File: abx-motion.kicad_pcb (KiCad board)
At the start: 4 copper layers, 157 x 105 mm, 203 parts, among them J1 XT60_BAT, J102 E_STOP, J201 USB-C, J202 ENC1_CONN, J203 ENC2_CONN, J204 CAN_TERM, J205 CAN_BUS, J206 RS485_TERM, J207 RS485_BUS, J208 OLED_I2C, J209 I2C_EXP, J301 MOTOR_OUT, J401 MOTOR_OUT, J501 STEP1_MOTOR, J502 STEP1_EXT, J503 STEP2_MOTOR, J504 STEP2_EXT, J505 RELAY1_OUT, J506 RELAY2_OUT, K501 G5LE-14-DC5, K502 G5LE-14-DC5, Q1 SQJ459EP-T1_GE3, Q301 CSD18540Q5B, Q302 CSD18540Q5B, Q303 CSD18540Q5B, Q304 CSD18540Q5B, Q401 CSD18540Q5B, Q402 CSD18540Q5B, Q403 CSD18540Q5B, Q404 CSD18540Q5B, Q501 AO3400A, Q502 AO3400A, SW201 RESET, SW202 BOOT, SW203 BTN_BACK, SW204 BTN_NEXT, SW205 BTN_HOME, SW501 MICROSTEP_CFG, SW502 MICROSTEP_CFG, U1 LMR36520FADDA, U2 AP2112K-3.3, U201 USBLC6-2SC6, U202 TCAN1042V-Q1, U203 THVD1450DR, U3 ESP32-S3-WROOM-1-N8R2, U301 DRV8701ERGER, U4 74LVC14A, U401 DRV8701ERGER, U501 StepStick_DRV8825, U502 StepStick_DRV8825

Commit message: Resolve all 5 prototype review items (F1 3557-2 4-pad THT, SMCJ30A, 2.2nF/0.5W snubber, 0.45-0.50mm stepper traces, clean PTH/NPTH drills)
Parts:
- C310, C410: value 10nF -> 2.2nF
- D2: value SMCJ28A -> SMCJ30A
- moved F1 5.55 mm to (167.6, 54.0)
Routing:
- net /Power_Supply/V_RAW_IN: track 32.2 -> 24.7 mm
- net /Power_Supply/V_FUSED: track 12.7 -> 17.7 mm
- net /Steppers_and_Relays/STEP2_A1: track 30.6 -> 31.5 mm
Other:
- board text added: "VBAT (J1 XT60): 12-32V (25A Fuse, Rev-Prot, SMCJ30A)"
- board text removed: "VBAT (J1 XT60): 12-32V (25A Fuse, Rev-Prot, SMCJ28A)"

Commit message: Release v1.0-production: finalize F1 3D STEP model alignment and archive V1.0 production package
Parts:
- F1: footprint Fuse:Fuse_Blade_ATO_directSolder -> abx-footprints:Fuseholder_Keystone_3557-2
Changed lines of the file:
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@@
 		)
 	)
-	(footprint "Fuse:Fuse_Blade_ATO_directSolder"
+	(footprint "abx-footprints:Fuseholder_Keystone_3557-2"
 		(layer "F.Cu")
 		(at 167.55 54)
@@
 		)
 		(embedded_fonts no)
-		(model "${KICAD9_3DMODEL_DIR}/Fuse.3dshapes/Fuseholder_Blade_Mini_Keystone_3568.step"
+		(model "${KIPRJMOD}/3dmodels/Fuseholder_Keystone_3557-2.step"
 			(offset
 				(xyz 0 0 0)

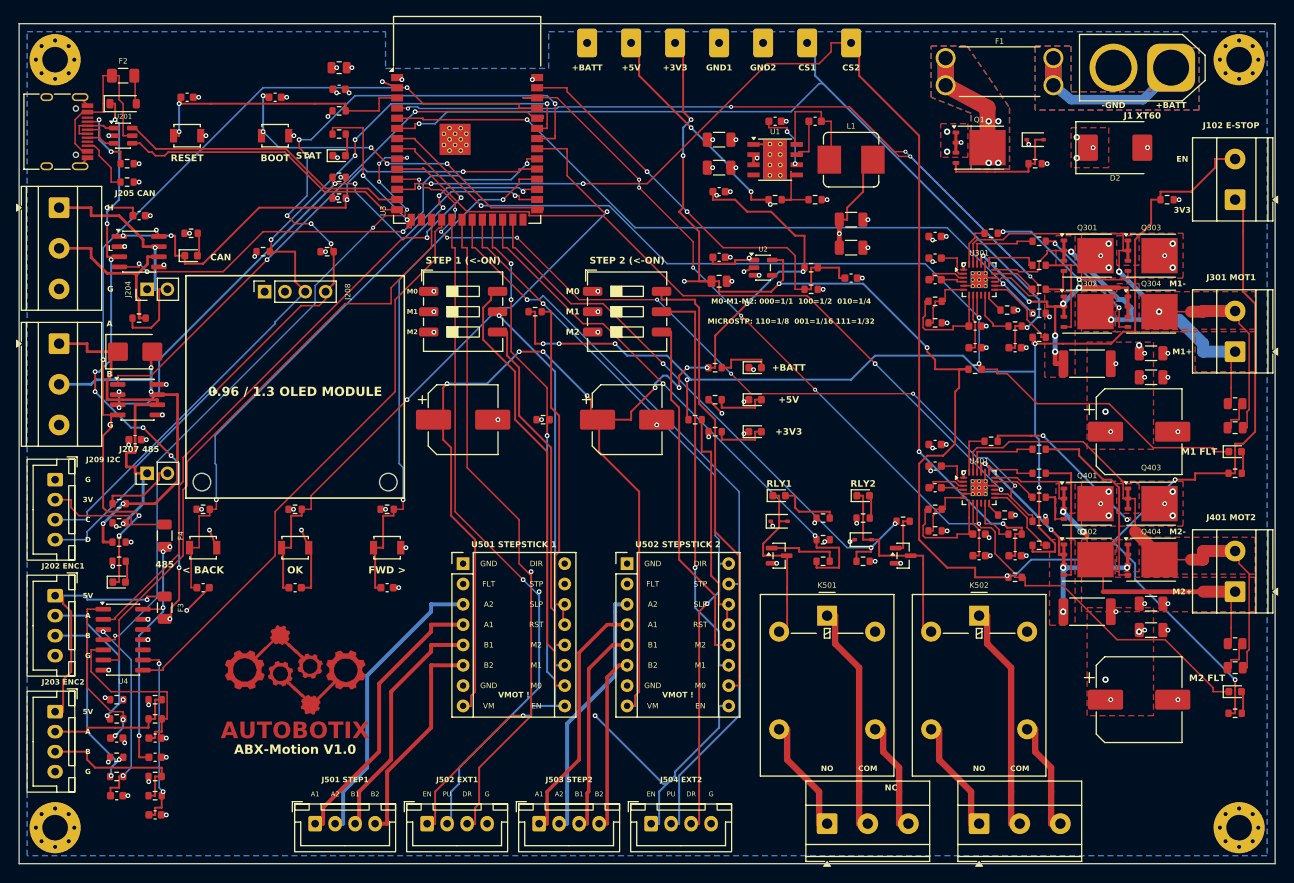
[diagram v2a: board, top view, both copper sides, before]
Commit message: Complete V1.1 compact 6-channel I/O & DC output architecture (0 ERC, 0 DRC errors, 0 unconnected, 0 parity)
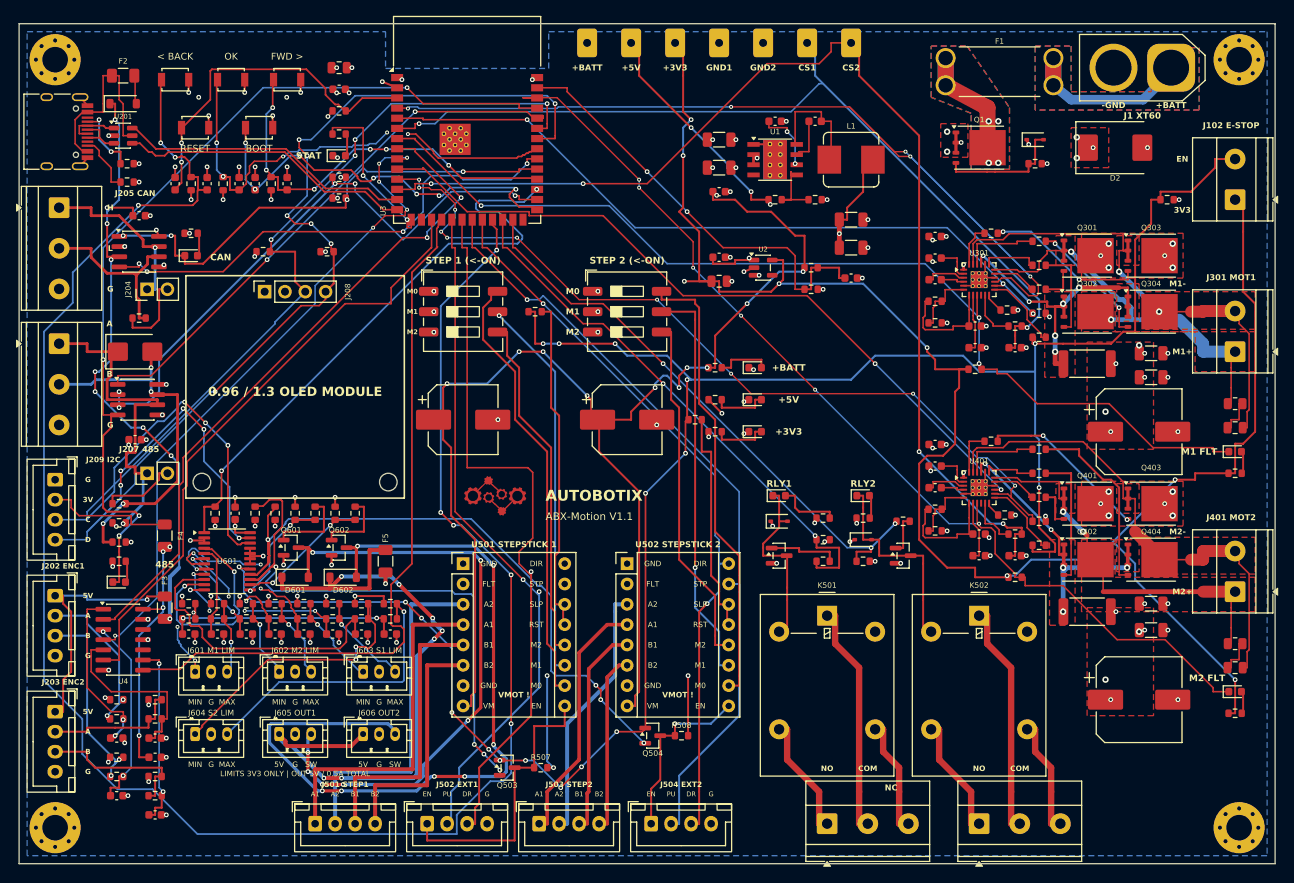
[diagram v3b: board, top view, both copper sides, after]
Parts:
- added C601: 100nF, Capacitor_SMD:C_0603_1608Metric, F.Cu at (72.0, 109.2)
- added C602: 10nF, Capacitor_SMD:C_0603_1608Metric, F.Cu at (66.2, 124.3)
- added C603: 10nF, Capacitor_SMD:C_0603_1608Metric, F.Cu at (69.8, 124.3)
- added C604: 10nF, Capacitor_SMD:C_0603_1608Metric, F.Cu at (73.4, 124.3)
- added C605: 10nF, Capacitor_SMD:C_0603_1608Metric, F.Cu at (77.0, 124.3)
- added C606: 10nF, Capacitor_SMD:C_0603_1608Metric, F.Cu at (80.6, 124.3)
- added C607: 10nF, Capacitor_SMD:C_0603_1608Metric, F.Cu at (84.2, 124.3)
- added C608: 10nF, Capacitor_SMD:C_0603_1608Metric, F.Cu at (87.8, 124.3)
- added C609: 10nF, Capacitor_SMD:C_0603_1608Metric, F.Cu at (91.4, 124.3)
- added D601: B5819W, Diode_SMD:D_SOD-123, F.Cu at (79.5, 117.2)
- added D602: B5819W, Diode_SMD:D_SOD-123, F.Cu at (85.5, 117.2)
- added F5: 500mA_PTC, Fuse:Fuse_1206_3216Metric, F.Cu at (90.8, 115.2)
- added J601: B3B-PH-K-S, Connector_JST:JST_PH_B3B-PH-K_1x03_P2.00mm_Vertical, F.Cu at (67.0, 129.0)
- added J602: B3B-PH-K-S, Connector_JST:JST_PH_B3B-PH-K_1x03_P2.00mm_Vertical, F.Cu at (77.5, 129.0)
- added J603: B3B-PH-K-S, Connector_JST:JST_PH_B3B-PH-K_1x03_P2.00mm_Vertical, F.Cu at (88.0, 129.0)
- added J604: B3B-PH-K-S, Connector_JST:JST_PH_B3B-PH-K_1x03_P2.00mm_Vertical, F.Cu at (67.0, 136.8)
- added J605: B3B-PH-K-S, Connector_JST:JST_PH_B3B-PH-K_1x03_P2.00mm_Vertical, F.Cu at (77.5, 136.8)
- added J606: B3B-PH-K-S, Connector_JST:JST_PH_B3B-PH-K_1x03_P2.00mm_Vertical, F.Cu at (88.0, 136.8)
- added Q503: AO3400A, Package_TO_SOT_SMD:SOT-23, F.Cu at (106.0, 141.0)
- added Q504: AO3400A, Package_TO_SOT_SMD:SOT-23, F.Cu at (124.2, 137.0)
- added Q601: AO3400A, Package_TO_SOT_SMD:SOT-23, F.Cu at (79.0, 113.5)
- added Q602: AO3400A, Package_TO_SOT_SMD:SOT-23, F.Cu at (85.0, 113.5)
- added R507: 10k, Resistor_SMD:R_0603_1608Metric, F.Cu at (110.2, 141.0)
- added R508: 10k, Resistor_SMD:R_0603_1608Metric, F.Cu at (127.8, 137.0)
- added R601: 4.7k, Resistor_SMD:R_0603_1608Metric, F.Cu at (66.2, 120.5)
- added R602: 4.7k, Resistor_SMD:R_0603_1608Metric, F.Cu at (69.8, 120.5)
- added R603: 4.7k, Resistor_SMD:R_0603_1608Metric, F.Cu at (73.4, 120.5)
- added R604: 4.7k, Resistor_SMD:R_0603_1608Metric, F.Cu at (77.0, 120.5)
- added R605: 4.7k, Resistor_SMD:R_0603_1608Metric, F.Cu at (80.6, 120.5)
- added R606: 4.7k, Resistor_SMD:R_0603_1608Metric, F.Cu at (84.2, 120.5)
- added R607: 4.7k, Resistor_SMD:R_0603_1608Metric, F.Cu at (87.8, 120.5)
- added R608: 4.7k, Resistor_SMD:R_0603_1608Metric, F.Cu at (91.4, 120.5)
- added R609: 1k, Resistor_SMD:R_0603_1608Metric, F.Cu at (66.2, 122.4)
- added R610: 1k, Resistor_SMD:R_0603_1608Metric, F.Cu at (69.8, 122.4)
- added R611: 1k, Resistor_SMD:R_0603_1608Metric, F.Cu at (73.4, 122.4)
- added R612: 1k, Resistor_SMD:R_0603_1608Metric, F.Cu at (77.0, 122.4)
- added R613: 1k, Resistor_SMD:R_0603_1608Metric, F.Cu at (80.6, 122.4)
- added R614: 1k, Resistor_SMD:R_0603_1608Metric, F.Cu at (84.2, 122.4)
- added R615: 1k, Resistor_SMD:R_0603_1608Metric, F.Cu at (87.8, 122.4)
- added R616: 1k, Resistor_SMD:R_0603_1608Metric, F.Cu at (91.4, 122.4)
- added R617: 1k, Resistor_SMD:R_0603_1608Metric, F.Cu at (79.5, 109.2)
- added R618: 1k, Resistor_SMD:R_0603_1608Metric, F.Cu at (84.5, 109.2)
- added R619: 100, Resistor_SMD:R_0603_1608Metric, F.Cu at (82.0, 109.2)
- added R620: 100, Resistor_SMD:R_0603_1608Metric, F.Cu at (87.0, 109.2)
- added R621: 10k, Resistor_SMD:R_0603_1608Metric, F.Cu at (74.5, 109.2)
- added R622: 10k, Resistor_SMD:R_0603_1608Metric, F.Cu at (77.0, 109.2)
- added U601: PCA9555PW,118, Package_SO:TSSOP-24_4.4x7.8mm_P0.65mm, F.Cu at (71.0, 115.2)
- moved LOGO2 95.3 mm to (164.0, 80.0)
- moved SW204 59.8 mm to (78.5, 55.0)
- moved SW205 59.0 mm to (71.5, 55.0)
- moved SW203 58.6 mm to (64.5, 55.0)
- moved C213 52.0 mm to (78.5, 68.0), turned to 90 degrees
- moved C214 51.0 mm to (72.5, 68.0), turned to 90 degrees
- moved C212 50.5 mm to (68.5, 68.0), turned to 90 degrees
- moved R228 43.2 mm to (76.5, 68.0), turned to 90 degrees
- moved R206 42.6 mm to (69.5, 109.2), turned to 90 degrees
- moved R229 41.7 mm to (70.5, 68.0), turned to 90 degrees
- moved R227 40.7 mm to (66.5, 68.0), turned to 90 degrees
- moved LOGO1 34.0 mm to (104.5, 108.0)
- moved C204 11.1 mm to (74.5, 68.0), turned to 90 degrees
- moved C203 10.9 mm to (64.5, 68.0), turned to 90 degrees
- moved SW202 2.24 mm to (75.0, 61.0)
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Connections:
- net /MCU_and_Encoders/I2C_SCL renamed /I2C_SCL
- net /MCU_and_Encoders/I2C_SDA renamed /I2C_SDA
- J502 pad 1: /STEP_ENABLE -> /Steppers_and_Relays/STEP1_EN_GATED
- J504 pad 1: /STEP_ENABLE -> /Steppers_and_Relays/STEP2_EN_GATED
- R206 pad 2: /STEP_ENABLE -> /IO_INT_N
- U3 pad 23: /STEP_ENABLE -> /MCU_and_Encoders/BTN_BACK
- U3 pad 29: /MCU_and_Encoders/BTN_BACK -> /IO_INT_N
- U501 pad 9: /STEP_ENABLE -> /Steppers_and_Relays/STEP1_EN_GATED
- U502 pad 9: /STEP_ENABLE -> /Steppers_and_Relays/STEP2_EN_GATED
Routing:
- net /MCU_and_Encoders/BTN_BACK: track 78.5 -> 241.6 mm, vias 4 -> 8
- net /STEP_ENABLE: track 129.7 -> 0.00 mm, vias 5 -> 0
- net /+3V3_DRV_EN: track 154.1 -> 267.9 mm, vias 6 -> 18
- net /Industrial_IO/OUT2_SW: track 0.00 -> 101.5 mm, vias 0 -> 7
- net /Industrial_IO/+5V_OUT: track 0.00 -> 89.6 mm, vias 0 -> 7
- net /STEP2_EN: track 0.00 -> 82.7 mm, vias 0 -> 4
- net /Industrial_IO/OUT1_SW: track 0.00 -> 77.4 mm, vias 0 -> 7
- net /IO_INT_N: track 0.00 -> 75.7 mm, vias 0 -> 2
- net /STEP1_EN: track 0.00 -> 72.7 mm, vias 0 -> 4
- net /I2C_SCL: track 101.0 -> 143.7 mm, vias 4 -> 7
- net /I2C_SDA: track 114.9 -> 155.9 mm, vias 7 -> 12
- net +3V3: track 272.4 -> 310.5 mm, vias 36 -> 49
- net /Industrial_IO/S2_MIN_IN: track 0.00 -> 37.1 mm
- net /Industrial_IO/S2_MAX_RAW: track 0.00 -> 36.7 mm, vias 0 -> 1
- net /Steppers_and_Relays/STEP1_EN_GATED: track 0.00 -> 36.1 mm
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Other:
- board text added: "ABX-MOTION V1.1 — SPECS & I/O REFERENCE"
- board text added: "ABX-Motion V1.1"
- board text added: "AUTOBOTIX"
- board text added: "AUX J605-J606: 5V / G / SW, 0.5A shared supply"
- board text added: "DC Servo 1&2: 2x 100W H-Bridge (DRV8701E, 15A Chop)"
- board text added: "E-Stop (J102): Hardware Gates DC Servos & Stepper EN"
- board text added: "J601 M1 LIM"
- board text added: "J602 M2 LIM"
- board text added: "J603 S1 LIM"
- board text added: "J604 S2 LIM"
- board text added: "J605 OUT1"
- board text added: "J606 OUT2"
- board text added: "LIMITS 3V3 ONLY | OUT 5V / 0.5A TOTAL"
- board text added: "LIMITS J601-J604: 8x dry contact / 3V3 logic ONLY"
- board text added: "MAX"
- board text added: "MIN"
- board text added: "Microstep (cont.): 001=1/16 101=1/32 111=1/32"
- board text added: "Microstep M0-M1-M2: 000=1 100=1/2 010=1/4 110=1/8"
- board text added: "Rails: +5V 2A Buck | +3.3V LDO | 4x PTC Polyfuses"
- board text added: "Relays (J505/506): 2x Omron G5LE SPDT | CAN & RS-485"
- board text added: "SW"
- board text added: "Steppers 1&2: StepStick + J501-J504 (Indep E-Stop EN)"
- board text removed: "ABX-MOTION V1.0 — SPECS & CONNECTIONS"
- board text removed: "Buses: CAN (J205) | RS-485 (J207) | I2C OLED"
- board text removed: "DC Servo 1&2: 2x 100W H-Bridge (DRV8701E, 15A)"
- board text removed: "E-Stop (J102): Loops +3V3 to +3V3_DRV_EN"
- board text removed: "M0-M1-M2: 000=1/1 100=1/2 010=1/4"
- board text removed: "MICROSTP: 110=1/8 001=1/16 111=1/32"
- board text removed: "Rails: +5V 2A Buck | +3.3V LDO | 3x PTC Polyfuses"
- board text removed: "Relays (J505/506): 2x Omron G5LE SPDT (10A)"
- board text removed: "Steppers 1&2: StepStick (<=36V) + J501-J504"
